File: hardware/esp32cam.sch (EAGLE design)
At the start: 32 parts, among them J1 MICRO_USB_B_HIROSE_ZX62-B-5PA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, J2 DM3AT-SF-PEJM5, SW1 TVAF06-A020B-R, X1 FA-238

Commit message: WIP
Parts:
- removed BOTTOM1, TOP1: P4_2.54, pins:P4_2.54
- removed C22: 0.1µ, rcl:C-EUC0402
- removed C23, C25, C26, C27, C28: (no value), rcl:C-EUC0402
- removed C24: 1µ, rcl:C-EUC0402
- removed FLASH1: W25Q32JVZPIQ, W25Q32JVZPIQ:W25Q32JVZPIQ
- removed LED3, LED4: (no value), led:LEDCHIPLED_0603
- removed R10, R8, R9: (no value), rcl:R-US_R0402
- removed R11, R12: 1k, rcl:R-US_R0402
- removed RP1: RP2040, RP2040:RP2040
- removed SW1: TVAF06-A020B-R, switches:TVAF06-A020B-R
- removed U$1: NJM12888F, regulators:NJM12888F
- removed X1: FA-238, crystal':FA-238
- added C1, C13, C4, C5, C6, C7: 0.1µF, rcl:C-EUC0402
- added C10, C9: P5_2.54, pins:P5_2.54
- added C11: 2.2µF, rcl:C-EUC0402
- added C12: 100pF, rcl:C-EUC0402
- added C14, C8: 0.01µF, rcl:C-EUC0402
- added C2: 10µF, rcl:C-EUC0402
- added C3: 22µF, rcl:C-EUC0402
- added CAM: OV2640_FPC_INV, camera:OV2640_FPC_INV
- added LED0, LED1: (no value), led:LEDCHIPLED_0603
- added Q1: HN1C01FU, transistors:HN1C01FU
- added R1, R2: (no value), rcl:R-US_R0402
- added R14: 1k, rcl:R-US_R0402
- added R3, R4, R5, R6: 10k, rcl:R-US_R0402
- added U$2: SPU0414HR5H-SB, microphones:SPU0414HR5H-SB
- added U1, U2: NJM11100, regulators:NJM11100
- added U3: FT234XD-R, FT234XD-R:FT234XD-R
- added U4: NJM12888F, regulators:NJM12888F
- added U5: ESP32-S3-WROOM-1-N16R2, ESP32-S3-WROOM-1-N16R2:ESP32-S3-WROOM-1-N16R2
- added VR1, VR2: (no value), potentiometers:PVZ3A
- added VR3: 100k, potentiometers:PVZ3A
- C15: value 0.1µ -> 1.0µF
- C16: value 0.1µ -> 100pF
- C17: value 0.1µF -> 15pF
- C18: value 10µF -> 0.1µF
- C19: value 1µ -> 0.1µF
- C20: value 0.1µ -> 2.2µF
- C21: value 0.1µ -> 10µF
- J2: device connector:DM3AT-SF-PEJM5 -> dm3at-sf-pejm5:DM3AT-SF-PEJM5
- R7: value (none) -> 10k
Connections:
- removed net 1V2: C24.1, C25.1, C26.1, RP1.DVDD, RP1.VREG_VOUT
- removed net ADC0: RP1.GPIO26/ADC0
- removed net ADC1: RP1.GPIO27/ADC1
- removed net ADC2: RP1.GPIO28/ADC2
- removed net ADC3: RP1.GPIO29/ADC3
- removed net I2C0_SDA: RP1.GPIO8
- removed net I2C1_SCL: RP1.GPIO7
- removed net I2C1_SDA: RP1.GPIO6
- removed net N$12: R12.1, SW1.B
- removed net PWM0_B: RP1.GPIO1
- removed net PWM1_A: RP1.GPIO2
- removed net PWM1_B: RP1.GPIO3
- removed net PWM3_A: RP1.GPIO22
- removed net PWM3_B: RP1.GPIO23
- removed net PWM4_A: RP1.GPIO24
- removed net PWM5_A: RP1.GPIO10
- removed net PWM5_B: RP1.GPIO11
- removed net QSPI_SCLK: FLASH1.CLK, RP1.QSPI_SCLK
- removed net QSPI_SD0: FLASH1.DI(IO0), RP1.QSPI_SD0
- removed net QSPI_SD1: FLASH1.DO(IO1), RP1.QSPI_SD1
- removed net QSPI_SD2: FLASH1.!WP!(IO2), RP1.QSPI_SD2
- removed net QSPI_SD3: FLASH1.!HOLD/RESET!(IO3), RP1.QSPI_SD3
- removed net QSPI_SS: FLASH1.!CS, R12.2, RP1.QSPI_CSN
- removed net SPI0_CS: RP1.GPIO21
- removed net SPI0_RX: RP1.GPIO20
- removed net SPI0_SCK: RP1.GPIO18
- removed net SPI0_TX: RP1.GPIO19
- removed net SPI1_CS: RP1.GPIO13
- removed net SPI1_RX: RP1.GPIO12
- removed net SPI1_SCK: RP1.GPIO14
- removed net SPI1_TX: RP1.GPIO15
- removed net SWCLK: RP1.SWCLK
- removed net SWD: RP1.SWD
- removed net USB_DM_1: R7.1, RP1.USB_DM
- removed net USB_DP_1: R8.1, RP1.USB_DP
- removed net XIN1: C27.1, RP1.XIN, X1.2
- removed net XOUT1: R11.2, RP1.XOUT
- new net 1.3V: C11.1, C12.1, CAM.DVDD, U1.VOUT, VR1.1
- new net 2.8V: C15.1, C16.1, C18.1, CAM.AVDD, CAM.DOVDD, R6.1, R7.2, U2.VOUT, VR2.1
- new net CAM_RESET: CAM.RST
- new net D0: CAM.D0
- new net D1: CAM.D1
- new net D2: CAM.D2
- new net D3: CAM.D3
- new net D4: CAM.D4
- new net D5: CAM.D5
- new net D6: CAM.D6
- new net D7: CAM.D7
- new net DTR: Q1G$2.E, R3.1
- new net EN: C6.1, Q1G$1.C, R5.1, U5.EN
- new net HSYNC: CAM.HREF
- new net I2C_SDA: CAM.SDA, R7.1, U5.IO5
- new net IO0: Q1G$2.C, U5.IO0
- new net MIC: U$2.OUTPUT, U5.IO1
- new net N$1: C8.1, U1.NB
- new net N$13: U$2.GAIN, VR3.2
- new net N$14: C20.1, VR3.3
- new net N$2: C12.2, U1.VADJ, VR1.2
- new net N$3: C14.1, U2.NB
- new net N$4: C16.2, U2.VADJ, VR2.2
- new net N$7: LED0.A, R1.1
- new net PCLK: C17.1, CAM.PCLK
- new net RTS: Q1G$1.E, R4.1, U3.RTS#
- new net RTX: U3.TXD, U5.RXD0
- new net SD: J2.A
- new net TRX: U3.RXD, U5.TXD0
- new net USB_VCC: D1.A, J1.+5V, U3.VCC
- new net VSYNC: CAM.VSYNC
- new net XCLK: CAM.XCLK
- net GND: now also C1.2, C10.1, C10.5, C11.2, C13.2, C14.2, C2.2, C3.2, C4.2, C5.2, C6.2, C7.2, C8.2, C9.1, C9.5, CAM.AGND, CAM.DGND, CAM.PAD1, CAM.PAD2, J2.B, J2.SHIELD, J2.VSS, LED0.C, LED1.C, R14.2, U$2.GND, U1.GND, U2.GND, U3.GND, U4.GND, U5.GND, VR1.3, VR2.3; no longer BOTTOM1.2, C16.2, C22.2, C23.2, C24.2, C25.2, C26.2, C27.2, C28.2, FLASH1.EXP, FLASH1.GND, LED3.C, LED4.C, RP1.GND, RP1.TESTEN, SW1.A, TOP1.2, U$1.GND, X1.G
- net I2C_SCL: now also CAM.SCL, R6.2, U5.IO4; no longer RP1.GPIO9
- net LED0: now also R1.2; no longer R9.2, RP1.GPIO0
- net LED1: now also R2.2; no longer R10.2, RP1.GPIO25
- net N$10: now also CAM.PWDN, R14.1; no longer LED4.A, R10.1
- net N$11: now also Q1G$2.B, R4.2; no longer C28.1, R11.1, X1.1
- net N$6: now also C5.1, U3.!RESET#, U3.3V3OUT, U3.VCCIO; no longer J1.ID
- net N$8: now also LED1.A, R2.1; no longer D1.A, J1.+5V
- net N$9: now also Q1G$1.B, R3.2; no longer LED3.A, R9.1
- net RX0: now also C9.4; no longer BOTTOM1.3, RP1.GPIO17
- net RX1: now also C10.4; no longer RP1.GPIO5, TOP1.3
- net TX0: now also C9.2; no longer BOTTOM1.4, RP1.GPIO16
- net TX1: now also C10.2; no longer RP1.GPIO4, TOP1.4
- net USB_DM: now also U3.USBDM; no longer R7.2
- net USB_DP: now also U3.USBDP; no longer R8.2
- net V+: now also C1.1, C10.3, C9.3, U4.CTRL, U4.VIN; no longer BOTTOM1.1, C17.1, TOP1.1, U$1.CTRL, U$1.VIN
- net VDD: now also C13.1, C2.1, C3.1, C4.1, C7.1, J2.VDD, R5.2, U$2.VDD, U1.CONTROL, U1.VIN, U2.CONTROL, U2.VIN, U4.VOUT, U5.3V3; no longer C15.1, C16.1, C18.1, C20.1, C22.1, C23.1, FLASH1.VCC, RP1.ADC_AVDD, RP1.IOVDD, RP1.USB_VDD, RP1.VREG_VIN, U$1.VOUT
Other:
- moved on the sheet: C15, C16, C17, C18, C19, C20, C21, D1, J1, R7

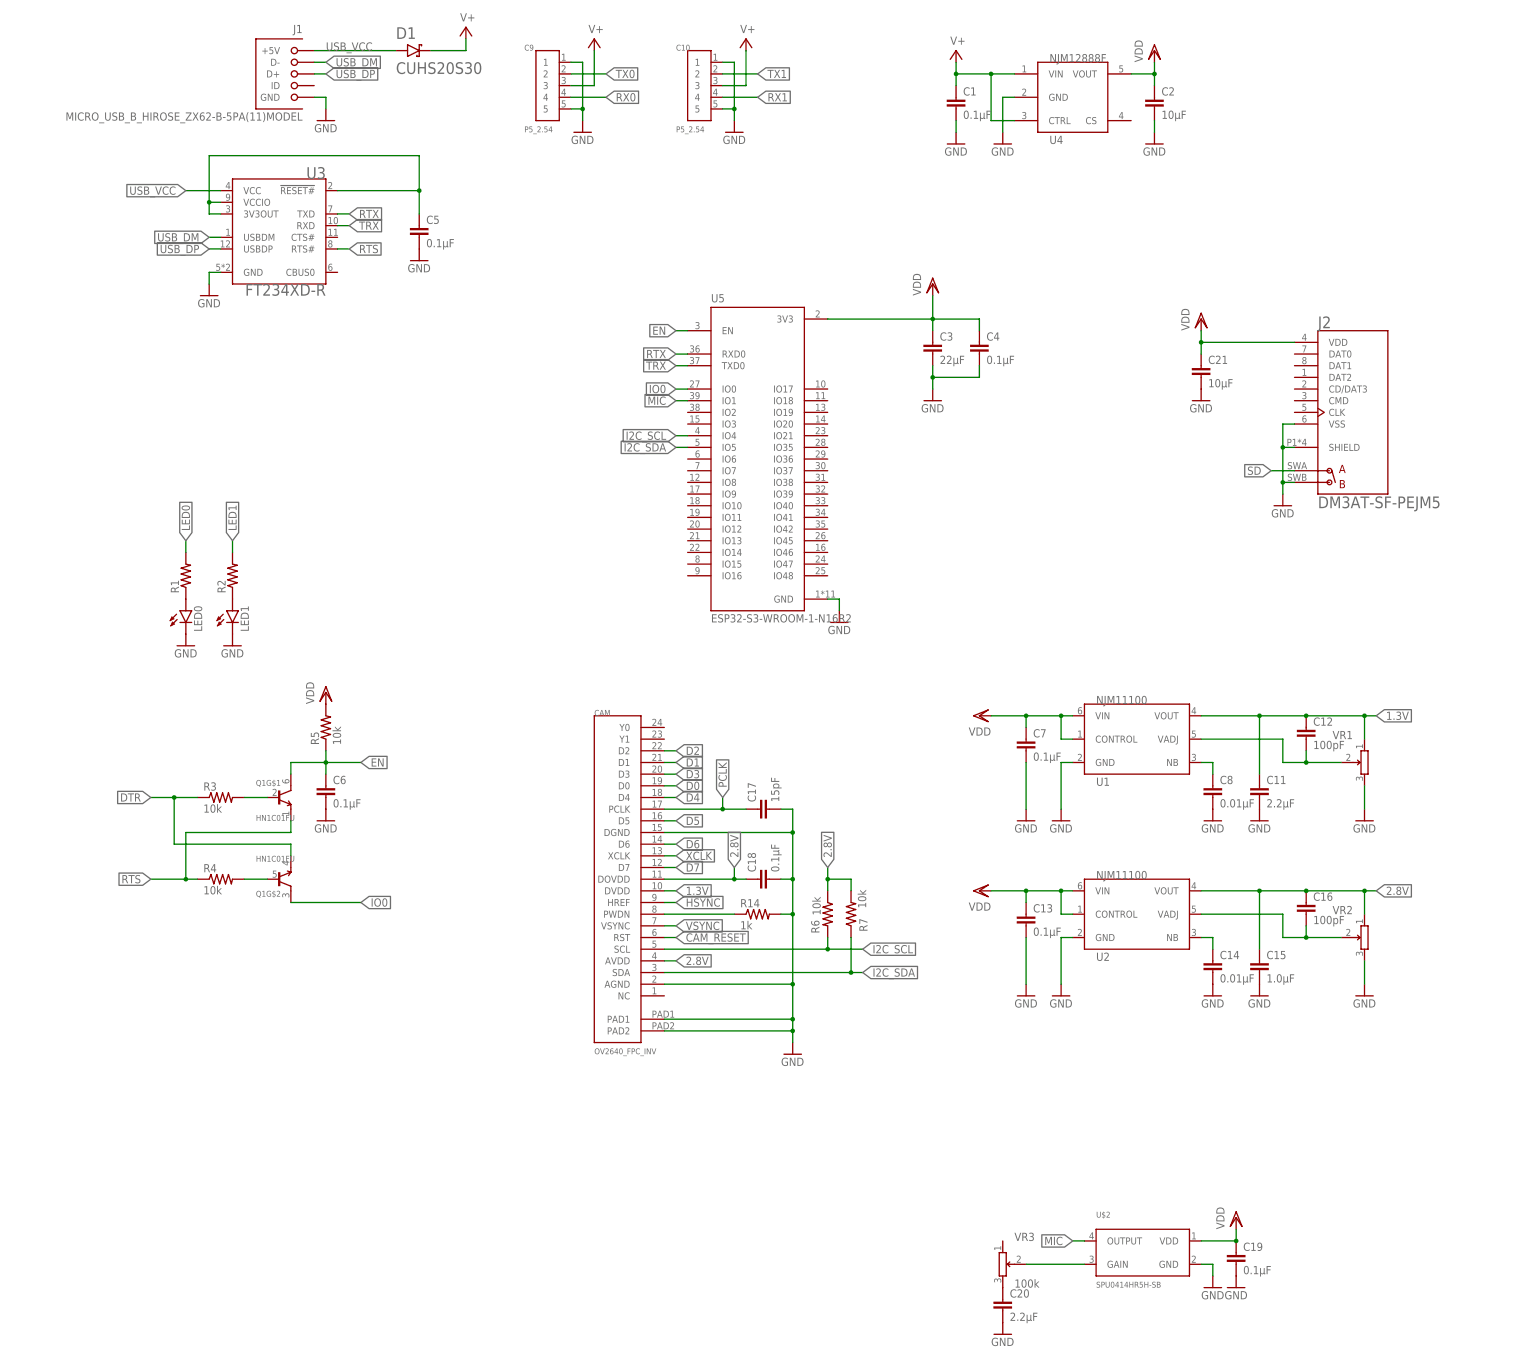
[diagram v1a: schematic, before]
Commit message: シルクを調整
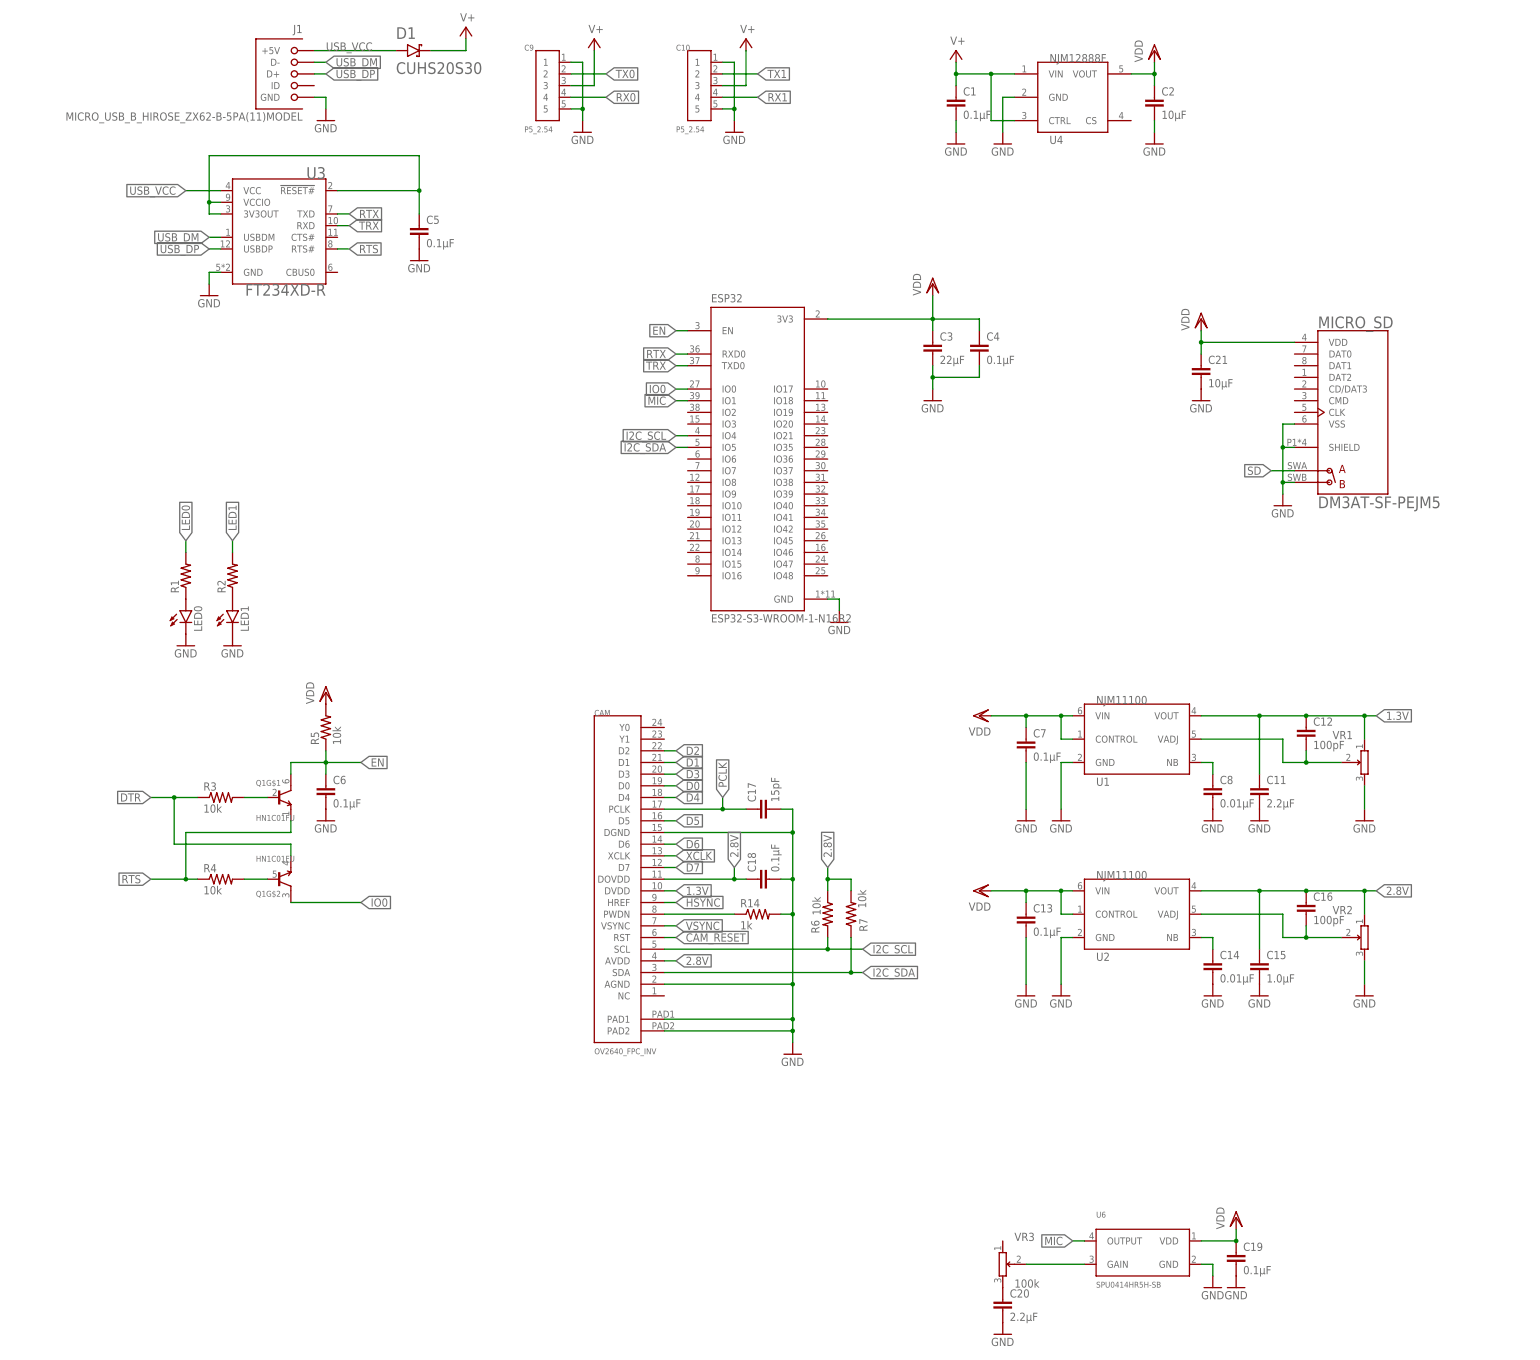
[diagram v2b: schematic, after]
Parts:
- renumbered J2 to MICRO_SD, U$2 to U6, U5 to ESP32
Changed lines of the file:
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@@
 <part name="VDD7" library="supply1" library_urn="urn:adsk.eagle:library:371" deviceset="VDD" device=""/>
 <part name="GND29" library="supply1" library_urn="urn:adsk.eagle:library:371" deviceset="GND" device=""/>
-<part name="J2" library="dm3at-sf-pejm5" deviceset="DM3AT-SF-PEJM5" device=""/>
+<part name="MICRO_SD" library="dm3at-sf-pejm5" deviceset="DM3AT-SF-PEJM5" device=""/>
 <part name="C3" library="rcl" library_urn="urn:adsk.eagle:library:334" deviceset="C-EU" device="C0402" package3d_urn="urn:adsk.eagle:package:23626/2" value="22µF"/>
 <part name="C4" library="rcl" library_urn="urn:adsk.eagle:library:334" deviceset="C-EU" device="C0402" package3d_urn="urn:adsk.eagle:package:23626/2" value="0.1µF"/>
@@
 <part name="GND15" library="supply1" library_urn="urn:adsk.eagle:library:371" deviceset="GND" device=""/>
 <part name="R14" library="rcl" library_urn="urn:adsk.eagle:library:334" deviceset="R-US_" device="R0402" package3d_urn="urn:adsk.eagle:package:23547/3" value="1k"/>
-<part name="U$2" library="microphones" deviceset="SPU0414HR5H-SB" device=""/>
+<part name="U6" library="microphones" deviceset="SPU0414HR5H-SB" device=""/>
 <part name="GND18" library="supply1" library_urn="urn:adsk.eagle:library:371" deviceset="GND" device=""/>
 <part name="VDD5" library="supply1" library_urn="urn:adsk.eagle:library:371" deviceset="VDD" device=""/>
@@
 <part name="VDD4" library="supply1" library_urn="urn:adsk.eagle:library:371" deviceset="VDD" device=""/>
 <part name="GND22" library="supply1" library_urn="urn:adsk.eagle:library:371" deviceset="GND" device=""/>
-<part name="U5" library="ESP32-S3-WROOM-1-N16R2" deviceset="ESP32-S3-WROOM-1-N16R2" device=""/>
+<part name="ESP32" library="ESP32-S3-WROOM-1-N16R2" deviceset="ESP32-S3-WROOM-1-N16R2" device=""/>
 <part name="GND25" library="supply1" library_urn="urn:adsk.eagle:library:371" deviceset="GND" device=""/>
 <part name="GND26" library="supply1" library_urn="urn:adsk.eagle:library:371" deviceset="GND" device=""/>
@@
 <attribute name="VALUE" x="22.86" y="147.32" size="1.778" layer="96"/>
 </instance>
-<instance part="J2" gate="G$1" x="228.6" y="116.84" smashed="yes">
+<instance part="MICRO_SD" gate="G$1" x="228.6" y="116.84" smashed="yes">
 <attribute name="NAME" x="220.98" y="135.1548" size="2.54433125" layer="95"/>
 <attribute name="VALUE" x="220.98" y="95.9862" size="2.54358125" layer="96"/>
@@
 <attribute name="VALUE" x="95.25" y="4.318" size="1.778" layer="96"/>
 </instance>
-<instance part="U$2" gate="G$1" x="182.88" y="-66.04" smashed="yes">
+<instance part="U6" gate="G$1" x="182.88" y="-66.04" smashed="yes">
 <attribute name="NAME" x="172.72" y="-58.42" size="1.27" layer="95"/>
 <attribute name="VALUE" x="172.72" y="-73.66" size="1.27" layer="96"/>
@@
 <attribute name="VALUE" x="193.04" y="116.84" size="1.778" layer="96"/>
 </instance>
-<instance part="U5" gate="G$1" x="99.06" y="106.68" smashed="yes">
+<instance part="ESP32" gate="G$1" x="99.06" y="106.68" smashed="yes">
 <attribute name="NAME" x="88.9" y="140.7922" size="1.778" layer="95"/>
 <attribute name="VALUE" x="88.9" y="71.12" size="1.778" layer="96"/>
@@
 </segment>
 <segment>
-<pinref part="U$2" gate="G$1" pin="GND"/>
+<pinref part="U6" gate="G$1" pin="GND"/>
 <wire x1="195.58" y1="-68.58" x2="198.12" y2="-68.58" width="0.1524" layer="91"/>
 <wire x1="198.12" y1="-68.58" x2="198.12" y2="-71.12" width="0.1524" layer="91"/>
@@
 </segment>
 <segment>
-<pinref part="U5" gate="G$1" pin="GND"/>
+<pinref part="ESP32" gate="G$1" pin="GND"/>
 <wire x1="114.3" y1="76.2" x2="116.84" y2="76.2" width="0.1524" layer="91"/>
 <wire x1="116.84" y1="76.2" x2="116.84" y2="73.66" width="0.1524" layer="91"/>
@@
 </segment>
 <segment>
-<pinref part="J2" gate="G$1" pin="B"/>
+<pinref part="MICRO_SD" gate="G$1" pin="B"/>
 <wire x1="215.9" y1="101.6" x2="213.36" y2="101.6" width="0.1524" layer="91"/>
 <wire x1="213.36" y1="101.6" x2="213.36" y2="99.06" width="0.1524" layer="91"/>
 <pinref part="GND27" gate="1" pin="GND"/>
-<pinref part="J2" gate="G$1" pin="SHIELD"/>
+<pinref part="MICRO_SD" gate="G$1" pin="SHIELD"/>
 <wire x1="215.9" y1="109.22" x2="213.36" y2="109.22" width="0.1524" layer="91"/>
 <wire x1="213.36" y1="109.22" x2="213.36" y2="101.6" width="0.1524" layer="91"/>
 <junction x="213.36" y="101.6"/>
-<pinref part="J2" gate="G$1" pin="VSS"/>
+<pinref part="MICRO_SD" gate="G$1" pin="VSS"/>
 <wire x1="215.9" y1="114.3" x2="213.36" y2="114.3" width="0.1524" layer="91"/>
 <wire x1="213.36" y1="114.3" x2="213.36" y2="109.22" width="0.1524" layer="91"/>
@@
 <pinref part="C3" gate="G$1" pin="1"/>
 <pinref part="C4" gate="G$1" pin="1"/>
-<pinref part="U5" gate="G$1" pin="3V3"/>
+<pinref part="ESP32" gate="G$1" pin="3V3"/>
 <wire x1="137.16" y1="137.16" x2="114.3" y2="137.16" width="0.1524" layer="91"/>
 </segment>
@@
 </segment>
 <segment>
-<pinref part="U$2" gate="G$1" pin="VDD"/>
+<pinref part="U6" gate="G$1" pin="VDD"/>
 <wire x1="203.2" y1="-63.5" x2="195.58" y2="-63.5" width="0.1524" layer="91"/>
 <wire x1="203.2" y1="-63.5" x2="203.2" y2="-60.96" width="0.1524" layer="91"/>
@@
 </segment>
 <segment>
-<pinref part="J2" gate="G$1" pin="VDD"/>
+<pinref part="MICRO_SD" gate="G$1" pin="VDD"/>
 <wire x1="215.9" y1="132.08" x2="195.58" y2="132.08" width="0.1524" layer="91"/>
 <wire x1="195.58" y1="132.08" x2="195.58" y2="134.62" width="0.1524" layer="91"/>
@@
 </segment>
 <segment>
-<pinref part="U5" gate="G$1" pin="TXD0"/>
+<pinref part="ESP32" gate="G$1" pin="TXD0"/>
 <wire x1="83.82" y1="127" x2="81.28" y2="127" width="0.1524" layer="91"/>
 <label x="81.28" y="127" size="1.778" layer="95" rot="R180" xref="yes"/>
@@
 </segment>
 <segment>
-<pinref part="U5" gate="G$1" pin="RXD0"/>
+<pinref part="ESP32" gate="G$1" pin="RXD0"/>
 <wire x1="83.82" y1="129.54" x2="81.28" y2="129.54" width="0.1524" layer="91"/>
 <label x="81.28" y="129.54" size="1.778" layer="95" rot="R180" xref="yes"/>
@@
 </segment>
 <segment>
-<pinref part="U5" gate="G$1" pin="EN"/>
+<pinref part="ESP32" gate="G$1" pin="EN"/>
 <wire x1="83.82" y1="134.62" x2="81.28" y2="134.62" width="0.1524" layer="91"/>
 <label x="81.28" y="134.62" size="1.778" layer="95" rot="R180" xref="yes"/>
@@
 </segment>
 <segment>
-<pinref part="U5" gate="G$1" pin="IO0"/>
+<pinref part="ESP32" gate="G$1" pin="IO0"/>
 <wire x1="83.82" y1="121.92" x2="81.28" y2="121.92" width="0.1524" layer="91"/>
 <label x="81.28" y="121.92" size="1.778" layer="95" rot="R180" xref="yes"/>
@@
 </segment>
 <segment>
-<pinref part="U5" gate="G$1" pin="IO4"/>
+<pinref part="ESP32" gate="G$1" pin="IO4"/>
 <wire x1="83.82" y1="111.76" x2="81.28" y2="111.76" width="0.1524" layer="91"/>
 <label x="81.28" y="111.76" size="1.778" layer="95" rot="R180" xref="yes"/>
@@
 </segment>
 <segment>
-<pinref part="U5" gate="G$1" pin="IO5"/>
+<pinref part="ESP32" gate="G$1" pin="IO5"/>
 <wire x1="83.82" y1="109.22" x2="81.28" y2="109.22" width="0.1524" layer="91"/>
 <label x="81.28" y="109.22" size="1.778" layer="95" rot="R180" xref="yes"/>
@@
 <net name="MIC" class="0">
 <segment>
-<pinref part="U$2" gate="G$1" pin="OUTPUT"/>
+<pinref part="U6" gate="G$1" pin="OUTPUT"/>
 <wire x1="170.18" y1="-63.5" x2="167.64" y2="-63.5" width="0.1524" layer="91"/>
 <label x="167.64" y="-63.5" size="1.778" layer="95" rot="R180" xref="yes"/>
 </segment>
 <segment>
-<pinref part="U5" gate="G$1" pin="IO1"/>
+<pinref part="ESP32" gate="G$1" pin="IO1"/>
 <wire x1="83.82" y1="119.38" x2="81.28" y2="119.38" width="0.1524" layer="91"/>
 <label x="81.28" y="119.38" size="1.778" layer="95" rot="R180" xref="yes"/>
@@
 <net name="N$13" class="0">
 <segment>
-<pinref part="U$2" gate="G$1" pin="GAIN"/>
+<pinref part="U6" gate="G$1" pin="GAIN"/>
 <wire x1="157.48" y1="-68.58" x2="170.18" y2="-68.58" width="0.1524" layer="91"/>
 <pinref part="VR3" gate="G$1" pin="2"/>
@@
 <net name="SD" class="0">
 <segment>
-<pinref part="J2" gate="G$1" pin="A"/>
+<pinref part="MICRO_SD" gate="G$1" pin="A"/>
 <wire x1="215.9" y1="104.14" x2="210.82" y2="104.14" width="0.1524" layer="91"/>
 <label x="210.82" y="104.14" size="1.778" layer="95" rot="R180" xref="yes"/>
